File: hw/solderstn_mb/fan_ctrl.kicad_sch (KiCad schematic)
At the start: 11 parts, among them M601 Fan_4pin, Q601 DMG1012T, U601 74LVC2G17gw

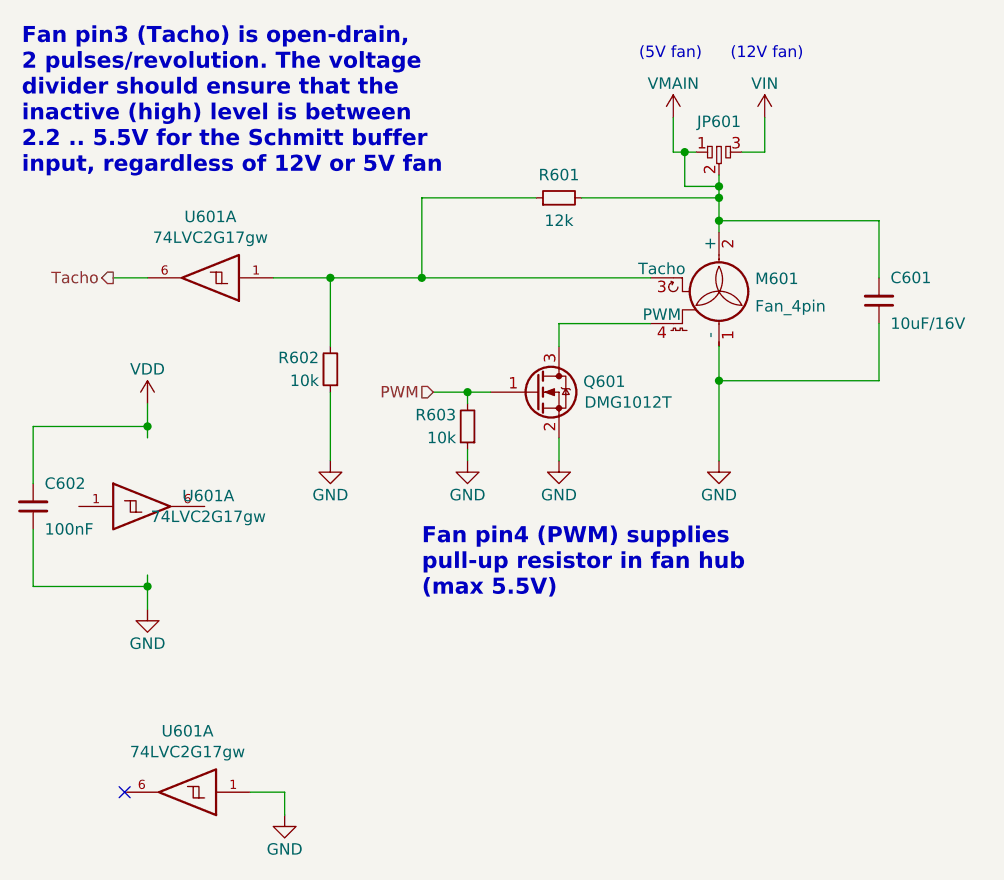
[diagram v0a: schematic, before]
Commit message: Placeholder 3d-models for rear-panel (w. conns), PSU, Bottom-plate, front-panel (w. conns), outer fp
With these placeholder mech. objects, the build-in 3d view of MB pcb features most of the mechanical
objects that constrain components placements. So 3d-view can be used to quickly check and iterate
placements to avoid 3d collisions, without having to first export MB STEP into FreeCAD and muck around
only to have to repeat again for each iteration
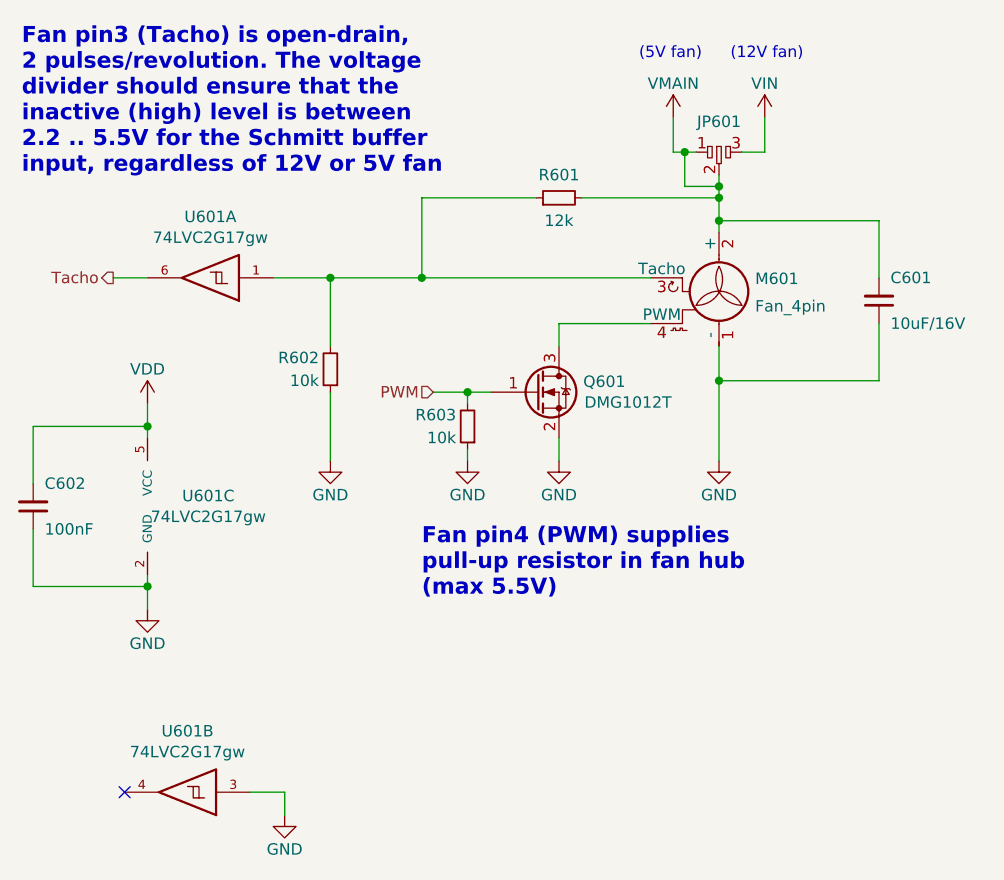
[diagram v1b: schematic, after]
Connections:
- net GND: now also U601.2 (GND), U601.3; no longer U601.1
- net VDD: now also U601.5 (VCC)
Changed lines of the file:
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@@
     (effects (font (size 1.27 1.27)) (justify right))
   )
-  (symbol (lib_id "customlib_mj:DMG1012T") (at 119.38 118.11 0)
+  (symbol (lib_id "customlib_mj:DMG1012T") (at 119.38 118.11 0) (unit 1)
     (in_bom yes) (on_board yes)
     (property "Reference" "Q601" (id 0) (at 124.6124 116.9416 0)
@@
     (pin "3")
   )
-  (symbol (lib_id "customlib_mj:74LVC2G17") (at 82.55 105.41 180)
+  (symbol (lib_id "customlib_mj:74LVC2G17") (at 82.55 105.41 180) (unit 1)
     (in_bom yes) (on_board yes)
     (property "Reference" "U601" (id 0) (at 83.185 98.6282 0))
@@
     (pin "6")
   )
-  (symbol (lib_id "customlib_mj:Fan_4pin") (at 139.7 107.95 0)
+  (symbol (lib_id "customlib_mj:Fan_4pin") (at 139.7 107.95 0) (unit 1)
     (in_bom yes) (on_board yes)
     (property "Reference" "M601" (id 0) (at 143.7132 105.5116 0)
@@
     (pin "4")
   )
-  (symbol (lib_id "customlib_mj:dogbone_3_ud") (at 139.7 91.44 0)
+  (symbol (lib_id "customlib_mj:dogbone_3_ud") (at 139.7 91.44 0) (unit 1)
     (in_bom yes) (on_board yes)
     (property "Reference" "JP601" (id 0) (at 139.7 88.0618 0))
@@
     (pin "3")
   )
-  (symbol (lib_id "power:GND") (at 139.7 125.73 0)
+  (symbol (lib_id "power:GND") (at 139.7 125.73 0) (unit 1)
     (in_bom yes) (on_board yes)
     (property "Reference" "#PWR0607" (id 0) (at 139.7 132.08 0)
@@
     (pin "1")
   )
-  (symbol (lib_id "customlib_mj:VIN") (at 144.78 87.63 0)
+  (symbol (lib_id "customlib_mj:VIN") (at 144.78 87.63 0) (unit 1)
     (in_bom yes) (on_board yes)
     (property "Reference" "#PWR0602" (id 0) (at 144.78 91.44 0)
@@
     (pin "1")
   )
-  (symbol (lib_id "customlib_mj:VMAIN") (at 134.62 87.63 0)
+  (symbol (lib_id "customlib_mj:VMAIN") (at 134.62 87.63 0) (unit 1)
     (in_bom yes) (on_board yes)
     (property "Reference" "#PWR0601" (id 0) (at 134.62 91.44 0)
@@
     (pin "1")
   )
-  (symbol (lib_id "power:GND") (at 121.92 125.73 0)
+  (symbol (lib_id "power:GND") (at 121.92 125.73 0) (unit 1)
     (in_bom yes) (on_board yes)
     (property "Reference" "#PWR0606" (id 0) (at 121.92 132.08 0)
@@
     (pin "1")
   )
-  (symbol (lib_id "Device:R_Small") (at 111.76 121.92 180)
+  (symbol (lib_id "Device:R_Small") (at 111.76 121.92 180) (unit 1)
     (in_bom yes) (on_board yes)
     (property "Reference" "R603" (id 0) (at 110.49 120.65 0)
@@
     (pin "2")
   )
-  (symbol (lib_id "power:GND") (at 111.76 125.73 0)
+  (symbol (lib_id "power:GND") (at 111.76 125.73 0) (unit 1)
     (in_bom yes) (on_board yes)
     (property "Reference" "#PWR0605" (id 0) (at 111.76 132.08 0)
@@
     (pin "1")
   )
-  (symbol (lib_id "Device:R_Small") (at 121.92 96.52 90)
+  (symbol (lib_id "Device:R_Small") (at 121.92 96.52 90) (unit 1)
     (in_bom yes) (on_board yes)
     (property "Reference" "R601" (id 0) (at 121.92 93.98 90))
@@
     (pin "2")
   )
-  (symbol (lib_id "Device:R_Small") (at 96.52 115.57 180)
+  (symbol (lib_id "Device:R_Small") (at 96.52 115.57 180) (unit 1)
     (in_bom yes) (on_board yes)
     (property "Reference" "R602" (id 0) (at 95.25 114.3 0)
@@
     (pin "2")
   )
-  (symbol (lib_id "power:GND") (at 96.52 125.73 0)
+  (symbol (lib_id "power:GND") (at 96.52 125.73 0) (unit 1)
     (in_bom yes) (on_board yes)
     (property "Reference" "#PWR0604" (id 0) (at 96.52 132.08 0)
@@
     (pin "1")
   )
-  (symbol (lib_id "customlib_mj:74LVC2G17") (at 76.2 130.81 0)
+  (symbol (lib_id "customlib_mj:74LVC2G17") (at 76.2 130.81 0) (unit 3)
     (in_bom yes) (on_board yes)
     (property "Reference" "U601" (id 0) (at 82.9564 129.6416 0))
@@
     (pin "5")
   )
-  (symbol (lib_id "power:VDD") (at 76.2 119.38 0)
+  (symbol (lib_id "power:VDD") (at 76.2 119.38 0) (unit 1)
     (in_bom yes) (on_board yes)
     (property "Reference" "#PWR0603" (id 0) (at 76.2 123.19 0)
@@
     (pin "1")
   )
-  (symbol (lib_id "power:GND") (at 76.2 142.24 0)
+  (symbol (lib_id "power:GND") (at 76.2 142.24 0) (unit 1)
     (in_bom yes) (on_board yes)
     (property "Reference" "#PWR0608" (id 0) (at 76.2 148.59 0)
@@
     (pin "1")
   )
-  (symbol (lib_id "Device:C_Small") (at 63.5 130.81 0) (mirror x)
+  (symbol (lib_id "Device:C_Small") (at 63.5 130.81 0) (mirror x) (unit 1)
     (in_bom yes) (on_board yes)
     (property "Reference" "C602" (id 0) (at 64.77 128.27 0)
@@
     (pin "2")
   )
-  (symbol (lib_id "Device:C_Small") (at 157.48 107.95 0) (mirror x)
+  (symbol (lib_id "Device:C_Small") (at 157.48 107.95 0) (mirror x) (unit 1)
     (in_bom yes) (on_board yes)
     (property "Reference" "C601" (id 0) (at 158.75 105.41 0)
@@
     (pin "2")
   )
-  (symbol (lib_id "customlib_mj:74LVC2G17") (at 80.01 162.56 180)
+  (symbol (lib_id "customlib_mj:74LVC2G17") (at 80.01 162.56 180) (unit 2)
     (in_bom yes) (on_board yes)
     (property "Reference" "U601" (id 0) (at 80.645 155.7782 0))
@@
     (pin "4")
   )
-  (symbol (lib_id "power:GND") (at 91.44 165.1 0)
+  (symbol (lib_id "power:GND") (at 91.44 165.1 0) (unit 1)
     (in_bom yes) (on_board yes)
     (property "Reference" "#PWR0609" (id 0) (at 91.44 171.45 0)

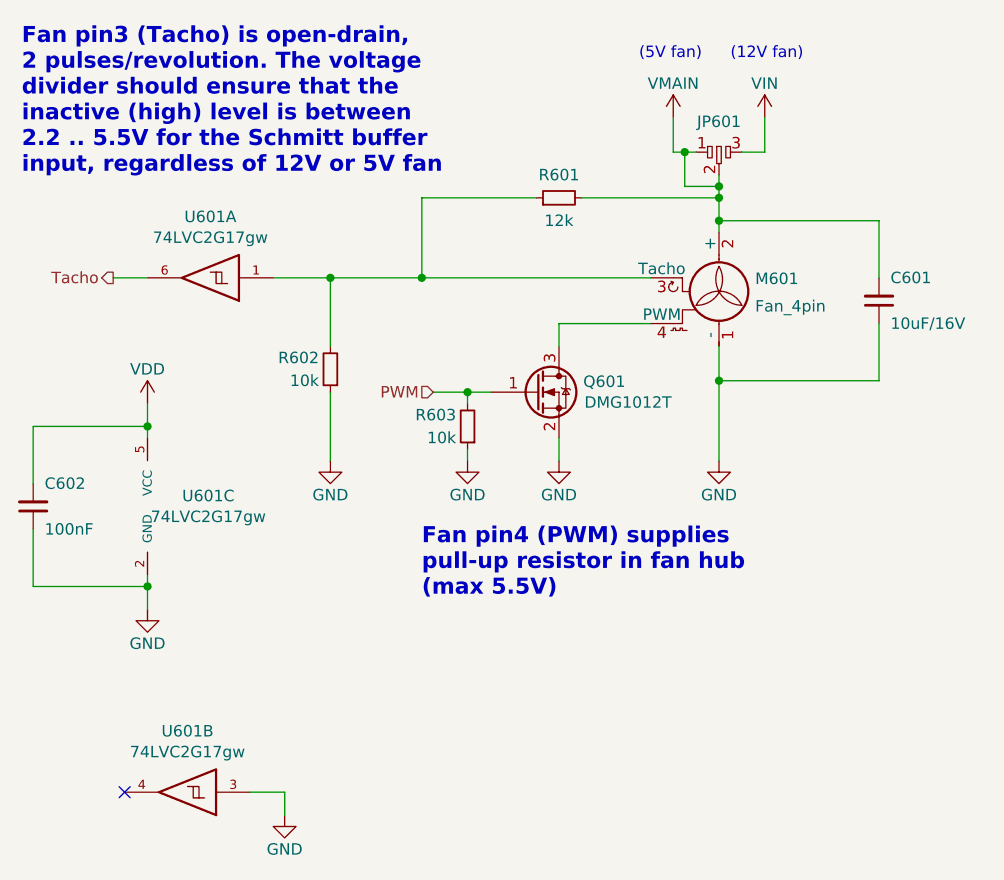
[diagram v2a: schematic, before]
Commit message: hw: long-standing uncommitted stuff; mostly auto-updates (v7) fw: remove L052 tree (CMSIS & std-HAL shouldn't be committed and it was the wrong device name anyway)
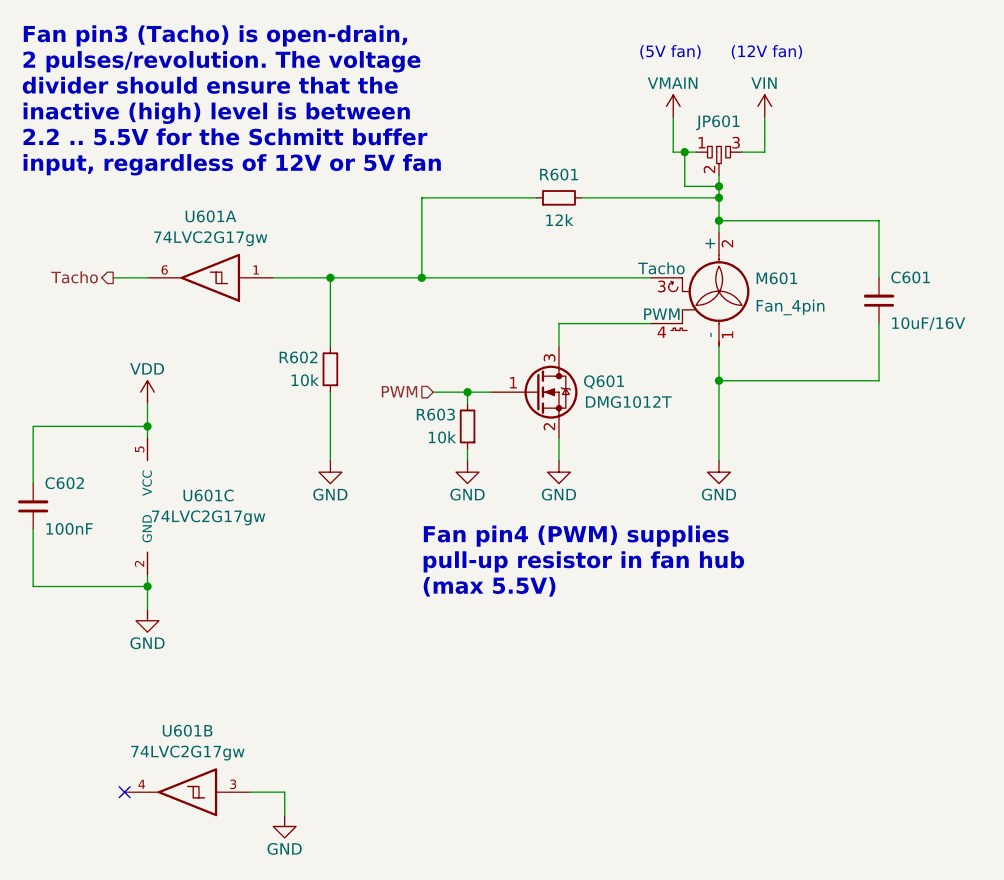
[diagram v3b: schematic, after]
